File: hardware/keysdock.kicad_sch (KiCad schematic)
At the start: 54 parts, among them J1 TYPE-C 16PFS 2JCB1.2-H6.5 IPX8, U1 ESP32-C6-WROOM-1-N8, U2 TLA2518IRTER, U3 TPS62142RGTR, U4 BQ24074RGTR, U5 TPD4E05U06DQAR, U6 TPS22910AYZVR

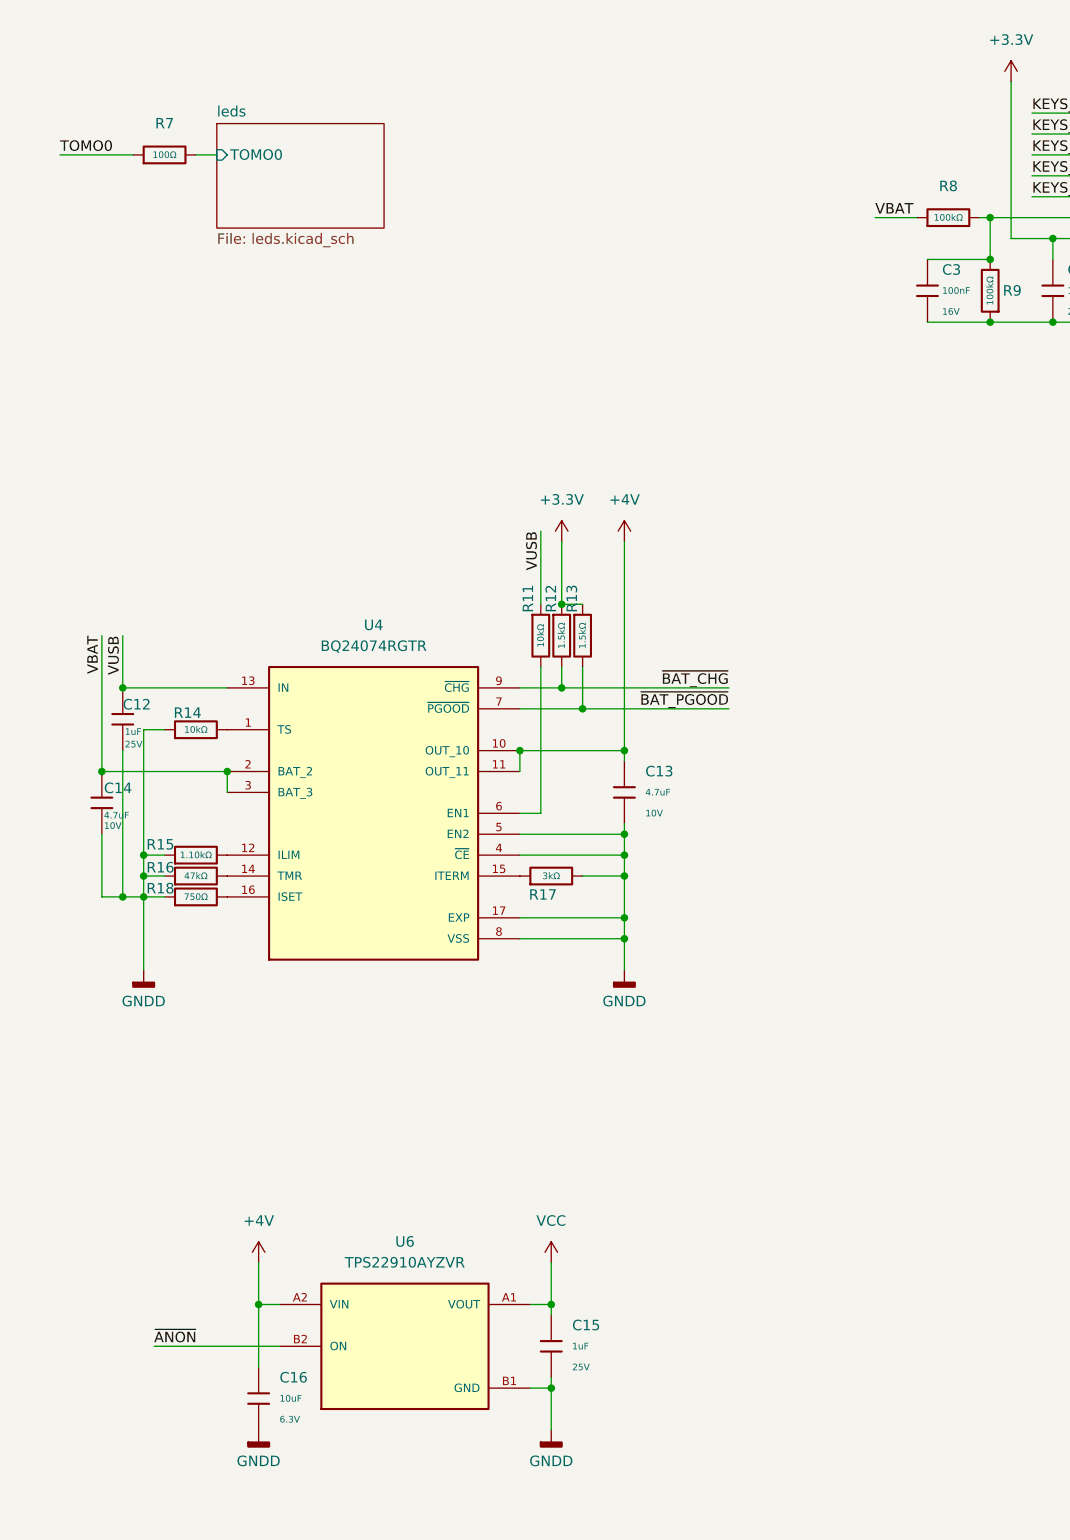
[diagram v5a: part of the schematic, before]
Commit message: :sparkles: add capacitor for LEDs
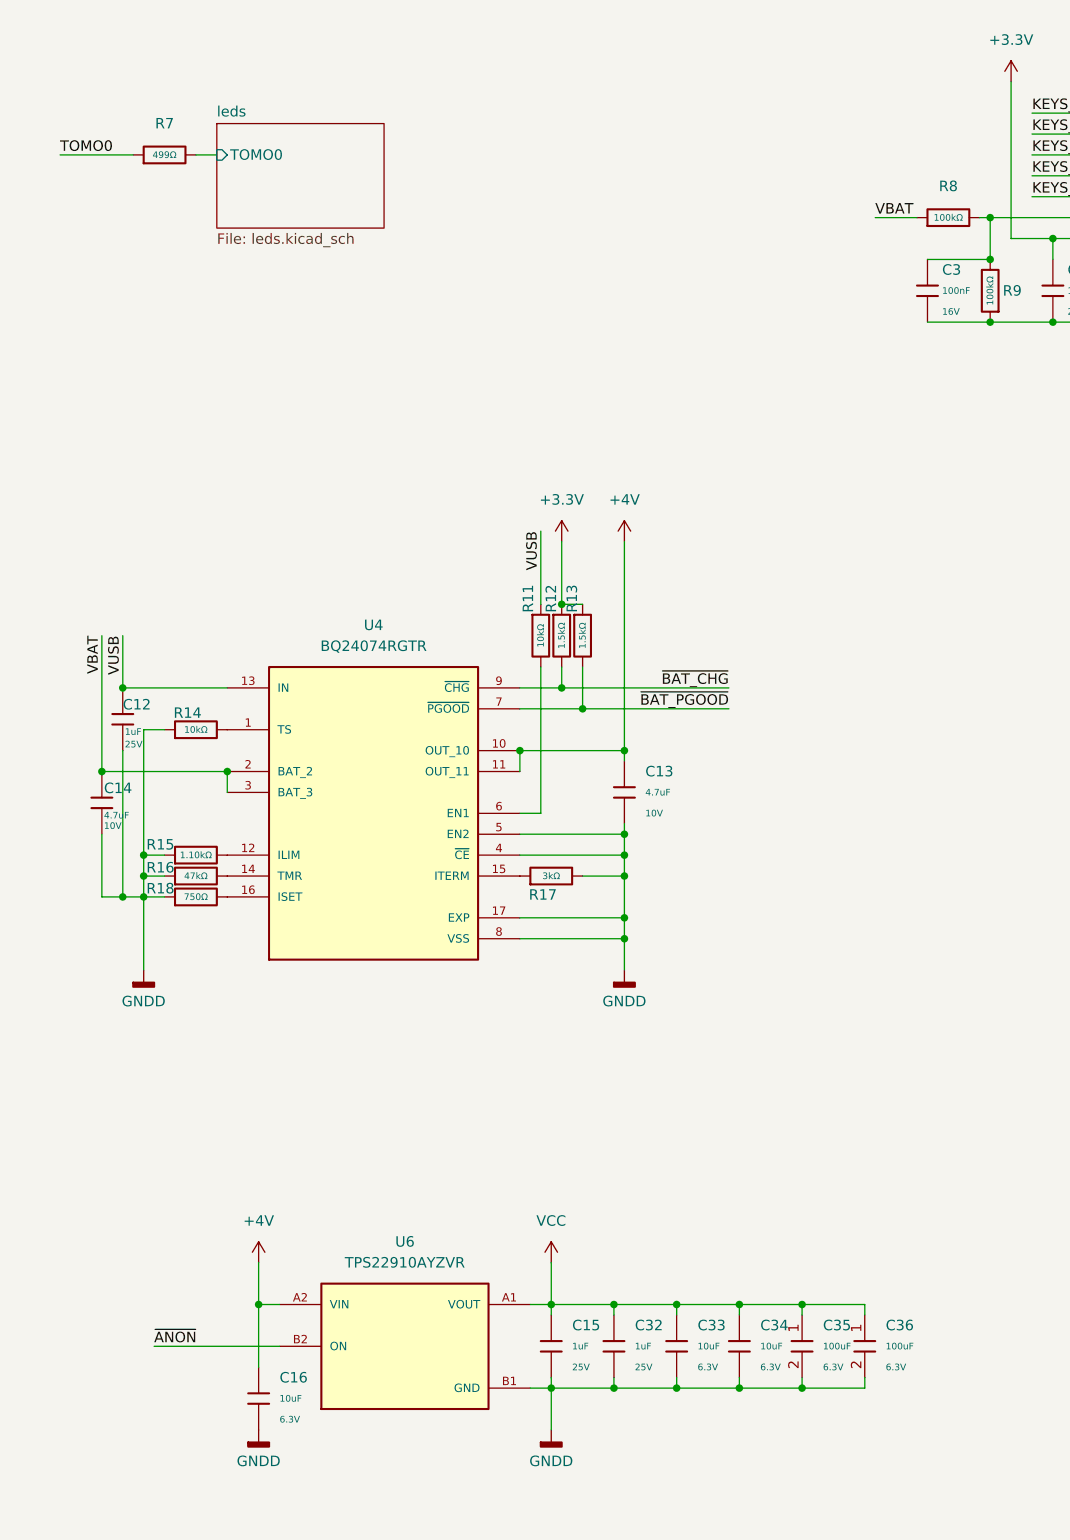
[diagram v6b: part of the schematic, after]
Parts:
- added C32: 1uF, KeysDock:C_0402, symbol KeysDock:0402,1uF
- added C33, C34: 10uF, KeysDock:C_0402, symbol KeysDock:0402,10uF
- added C35, C36: 100uF, KeysDock:C_1206, symbol KeysDock:1206,100uF
- R7: value 100Ω -> 499Ω; symbol KeysDock:0402,100Ω -> KeysDock:0402,499Ω; LCSC C25076 -> C4125; Part 0402WGF1000TCE -> 0402WGF4990TCE; Resistance 100Ω -> 499Ω; Stock 5907585 -> 7644059; Temperature Coefficient ±200ppm/°C -> ±100ppm/°C
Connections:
- net GND: now also C32.2, C33.2, C34.2, C35.2, C36.2
- net VCC: now also C32.1, C33.1, C34.1, C35.1, C36.1

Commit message: :construction: init spice tests
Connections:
- net GND: no longer C2.2, U2.15 (AIN0/GPIO0), U2.16 (AIN1/GPIO1), U2.17 (GND), U2.9 (GND)
- net GNDA: now also C2.2, U2.15 (AIN0/GPIO0), U2.16 (AIN1/GPIO1), U2.17 (GND), U2.9 (GND)
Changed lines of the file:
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@@
 	)
 	(symbol
-		(lib_id "power:GNDD")
-		(at 355.6 132.08 0)
-		(unit 1)
-		(body_style 1)
-		(exclude_from_sim no)
-		(in_bom yes)
-		(on_board yes)
-		(in_pos_files yes)
-		(dnp no)
-		(fields_autoplaced yes)
-		(property "Reference" "#PWR015"
-			(at 355.6 138.43 0)
-			(hide yes)
-			(show_name no)
-			(do_not_autoplace no)
-			(effects
-				(font
-					(size 1.27 1.27)
-				)
-			)
-		)
-		(property "Value" "GNDD"
-			(at 355.6 135.89 0)
-			(show_name no)
-			(do_not_autoplace no)
-			(effects
-				(font
-					(size 1.27 1.27)
-				)
-			)
-		)
-		(property "Footprint" ""
-			(at 355.6 132.08 0)
-			(hide yes)
-			(show_name no)
-			(do_not_autoplace no)
-			(effects
-				(font
-					(size 1.27 1.27)
-				)
-			)
-		)
-		(property "Datasheet" ""
-			(at 355.6 132.08 0)
-			(hide yes)
-			(show_name no)
-			(do_not_autoplace no)
-			(effects
-				(font
-					(size 1.27 1.27)
-				)
-			)
-		)
-		(property "Description" "Power symbol creates a global label with name \"GNDD\" , digital ground"
-			(at 355.6 132.08 0)
-			(hide yes)
-			(show_name no)
-			(do_not_autoplace no)
-			(effects
-				(font
-					(size 1.27 1.27)
-				)
-			)
-		)
-		(pin "1"
-		)
-		(instances
-			(project "keysdock"
-				(path "/1dbf2a4e-9b9b-4b09-9979-c8b99f6b5d2a"
-					(reference "#PWR015")
-					(unit 1)
-				)
-			)
-		)
-	)
-	(symbol
 		(lib_id "KeysDock:0402,22Ω")
 		(at 86.36 251.46 0)
@@
 					(unit 1)
 				)
+			)
+		)
+	)
+	(symbol
+		(lib_id "power:GNDA")
+		(at 355.6 132.08 0)
+		(unit 1)
+		(body_style 1)
+		(exclude_from_sim no)
+		(in_bom yes)
+		(on_board yes)
+		(in_pos_files yes)
+		(dnp no)
+		(fields_autoplaced yes)
+		(property "Reference" "#PWR015"
+			(at 355.6 138.43 0)
+			(hide yes)
+			(show_name no)
+			(do_not_autoplace no)
+			(effects
+				(font
+					(size 1.27 1.27)
+				)
+			)
+		)
+		(property "Value" "GNDA"
+			(at 355.6 137.16 0)
+			(show_name no)
+			(do_not_autoplace no)
+			(effects
+				(font
+					(size 1.27 1.27)
+				)
+			)
+		)
+		(property "Footprint" ""
+			(at 355.6 132.08 0)
+			(hide yes)
+			(show_name no)
+			(do_not_autoplace no)
+			(effects
+				(font
+					(size 1.27 1.27)
+				)
+			)
+		)
+		(property "Datasheet" ""
+			(at 355.6 132.08 0)
+			(hide yes)
+			(show_name no)
+			(do_not_autoplace no)
+			(effects
+				(font
+					(size 1.27 1.27)
+				)
+			)
+		)
+		(property "Description" "Power symbol creates a global label with name \"GNDA\" , analog ground"
+			(at 355.6 132.08 0)
+			(hide yes)
+			(show_name no)
+			(do_not_autoplace no)
+			(effects
+				(font
+					(size 1.27 1.27)
+				)
+			)
+		)
+		(pin "1"
+		)
+		(instances
+			(project "keysdock"
+				(path "/1dbf2a4e-9b9b-4b09-9979-c8b99f6b5d2a"
+					(reference "#PWR015")
+					(unit 1)
+				)
